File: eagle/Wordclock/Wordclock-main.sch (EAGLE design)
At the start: 36 parts, among them IC1 MEGA8-P, J1 AVR_SPI_PRG_6PTH, Q1 16MHz

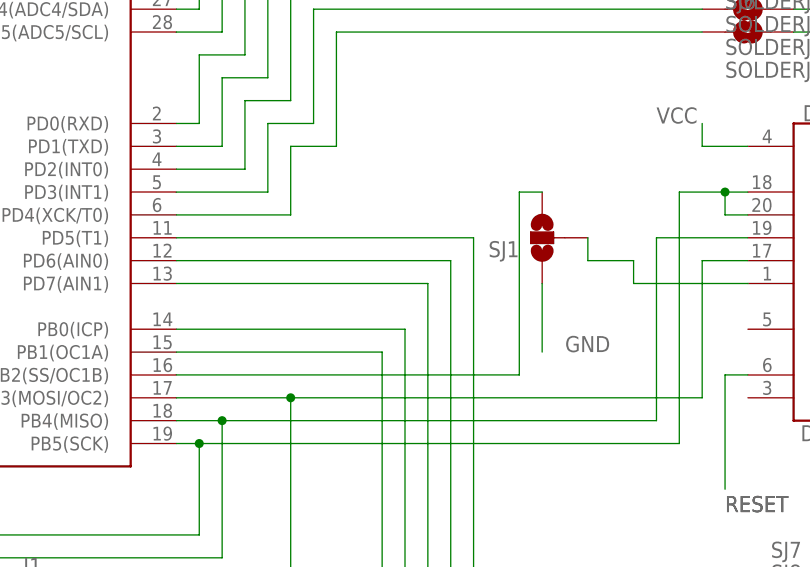
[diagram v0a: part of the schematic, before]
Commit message: Wordclock main : v1.1 with still wrong DS3231
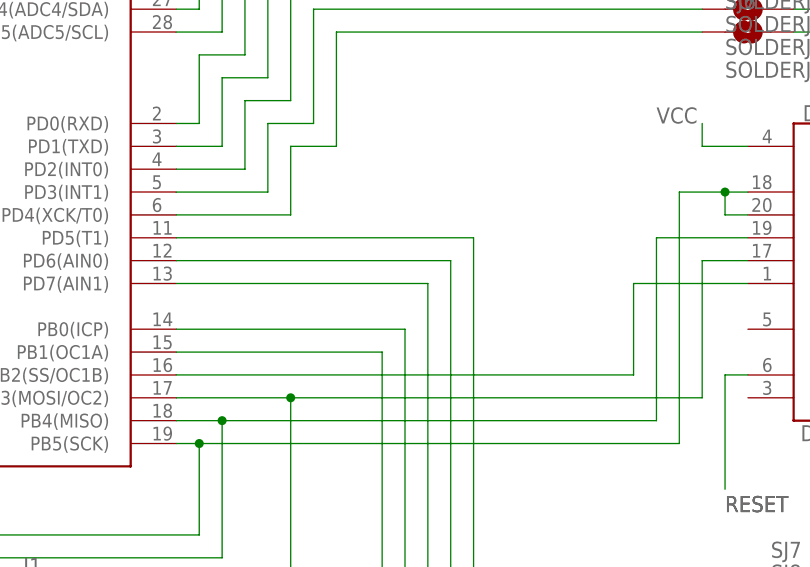
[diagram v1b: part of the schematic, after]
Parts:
- removed SJ1: (no value), SparkFun:SOLDERJUMPER_2WAYT
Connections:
- removed net N$2: DS3234.CS, SJ1.2
- net GND: no longer SJ1.1
- net N$6: now also DS3234.CS; no longer SJ1.3
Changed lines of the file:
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@@
 <part name="JPEAST" library="SparkFun" deviceset="M05" device="PTH"/>
 <part name="JPSOUTH" library="SparkFun" deviceset="M05" device="PTH"/>
-<part name="SJ1" library="SparkFun" deviceset="SOLDERJUMPER_2WAY" device="T"/>
 <part name="UNREGULATED" library="SparkFun" deviceset="M02" device="PTH3"/>
 <part name="BAT1" library="SparkFun" deviceset="BATTERY" device="20PTH"/>
@@
 <instance part="JPEAST" gate="G$1" x="195.58" y="5.08" rot="R180"/>
 <instance part="JPSOUTH" gate="G$1" x="190.5" y="76.2" rot="R180"/>
-<instance part="SJ1" gate="G$1" x="149.86" y="48.26" rot="R180"/>
 <instance part="UNREGULATED" gate="G$1" x="-17.78" y="20.32"/>
 <instance part="BAT1" gate="G$1" x="-66.04" y="20.32"/>
@@
 </segment>
 <segment>
-<pinref part="SJ1" gate="G$1" pin="1"/>
-<wire x1="149.86" y1="43.18" x2="149.86" y2="35.56" width="0.1524" layer="91"/>
-<label x="152.4" y="35.56" size="1.778" layer="95"/>
-</segment>
-<segment>
 <pinref part="UNREGULATED" gate="G$1" pin="1"/>
 <wire x1="-10.16" y1="20.32" x2="-10.16" y2="15.24" width="0.1524" layer="91"/>
@@
 </segment>
 </net>
-<net name="N$2" class="0">
-<segment>
-<wire x1="160.02" y1="45.72" x2="160.02" y2="43.18" width="0.1524" layer="91"/>
-<pinref part="DS3234" gate="G$1" pin="CS"/>
-<wire x1="160.02" y1="43.18" x2="172.72" y2="43.18" width="0.1524" layer="91"/>
-<pinref part="SJ1" gate="G$1" pin="2"/>
-<wire x1="160.02" y1="45.72" x2="154.94" y2="45.72" width="0.1524" layer="91"/>
-<wire x1="154.94" y1="45.72" x2="154.94" y2="48.26" width="0.1524" layer="91"/>
-</segment>
-</net>
 <net name="RESET" class="0">
 <segment>
@@
 <segment>
 <pinref part="IC1" gate="G$1" pin="PB2(SS/OC1B)"/>
-<wire x1="109.22" y1="33.02" x2="147.32" y2="33.02" width="0.1524" layer="91"/>
-<wire x1="147.32" y1="33.02" x2="147.32" y2="53.34" width="0.1524" layer="91"/>
-<pinref part="SJ1" gate="G$1" pin="3"/>
-<wire x1="147.32" y1="53.34" x2="149.86" y2="53.34" width="0.1524" layer="91"/>
-</segment>
-</net>
+<wire x1="109.22" y1="33.02" x2="160.02" y2="33.02" width="0.1524" layer="91"/>
+<pinref part="DS3234" gate="G$1" pin="CS"/>
+<wire x1="160.02" y1="43.18" x2="172.72" y2="43.18" width="0.1524" layer="91"/>
+<wire x1="160.02" y1="33.02" x2="160.02" y2="43.18" width="0.1524" layer="91"/>
+</segment>
+</net>

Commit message: v1.1 with corrected DS3231 package : a SO16W(ide)
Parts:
- U$1: value DS3231 -> DS3231DS3231-SO16W; device DS3231:DS3231 -> kalshagar:DS3231DS3231-SO16W
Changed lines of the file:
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@@
 <parts>
 <part name="IC1" library="atmel" deviceset="MEGA8-P" device=""/>
-<part name="U$1" library="DS3231" deviceset="DS3231" device=""/>
+<part name="U$1" library="kalshagar" deviceset="DS3231" device="DS3231-SO16W"/>
 <part name="5V" library="SparkFun" deviceset="M02" device="PTH3"/>
 <part name="PUSCL" library="resistor" deviceset="R-EU_" device="0204/5" value="10k"/>
